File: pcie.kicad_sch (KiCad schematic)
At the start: 14 parts, among them J9 PCB-Edge_M.2_Key-M

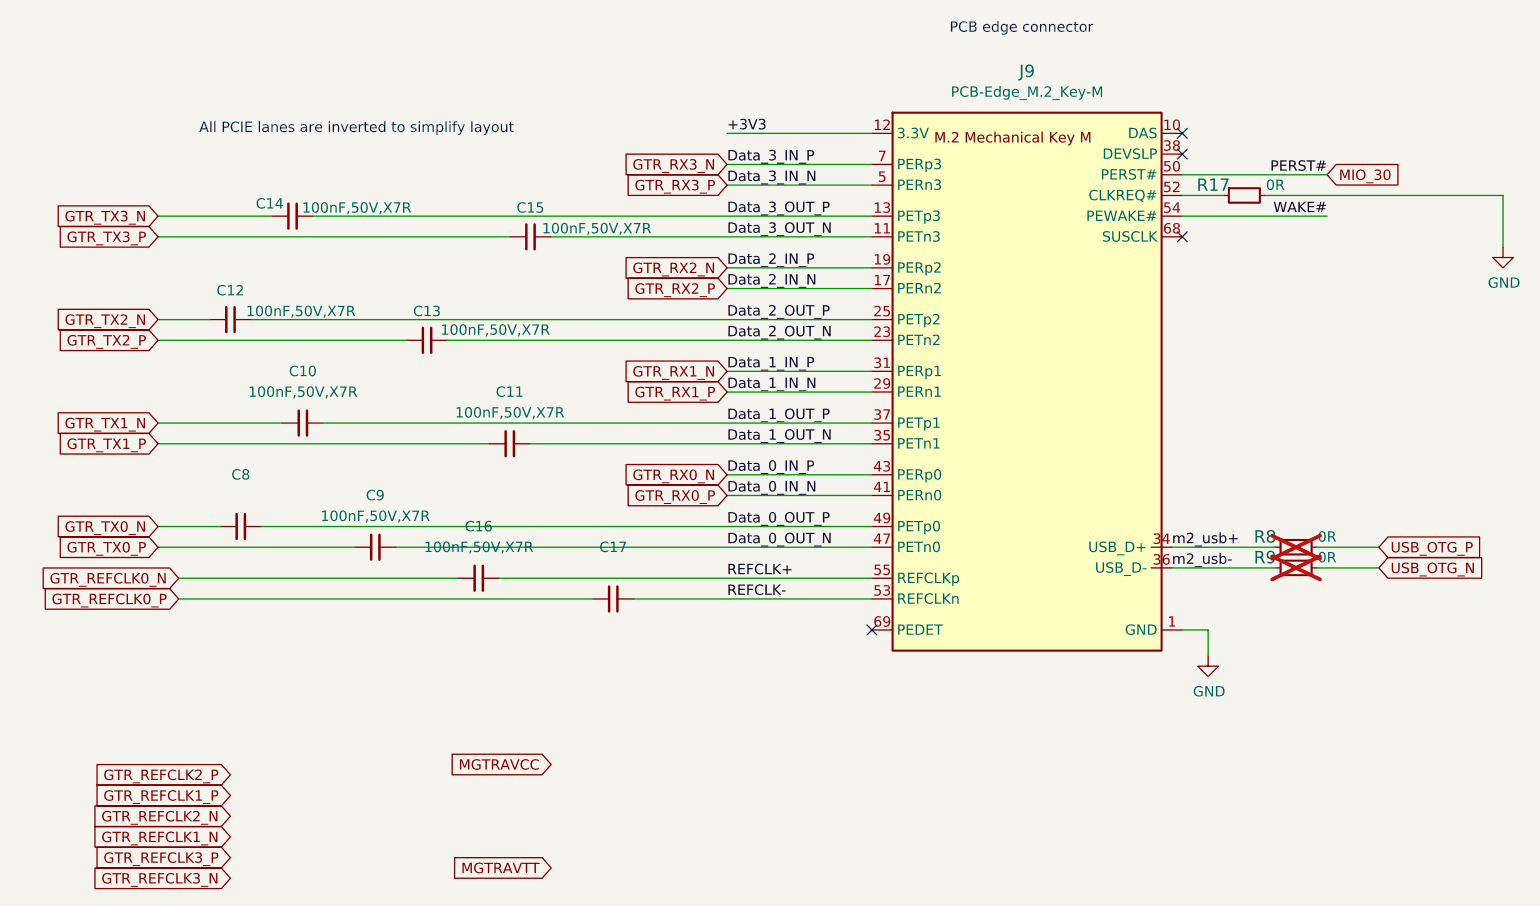
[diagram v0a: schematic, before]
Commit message: moved jtag connector, added holes for all power supplies, fixed most of DRC
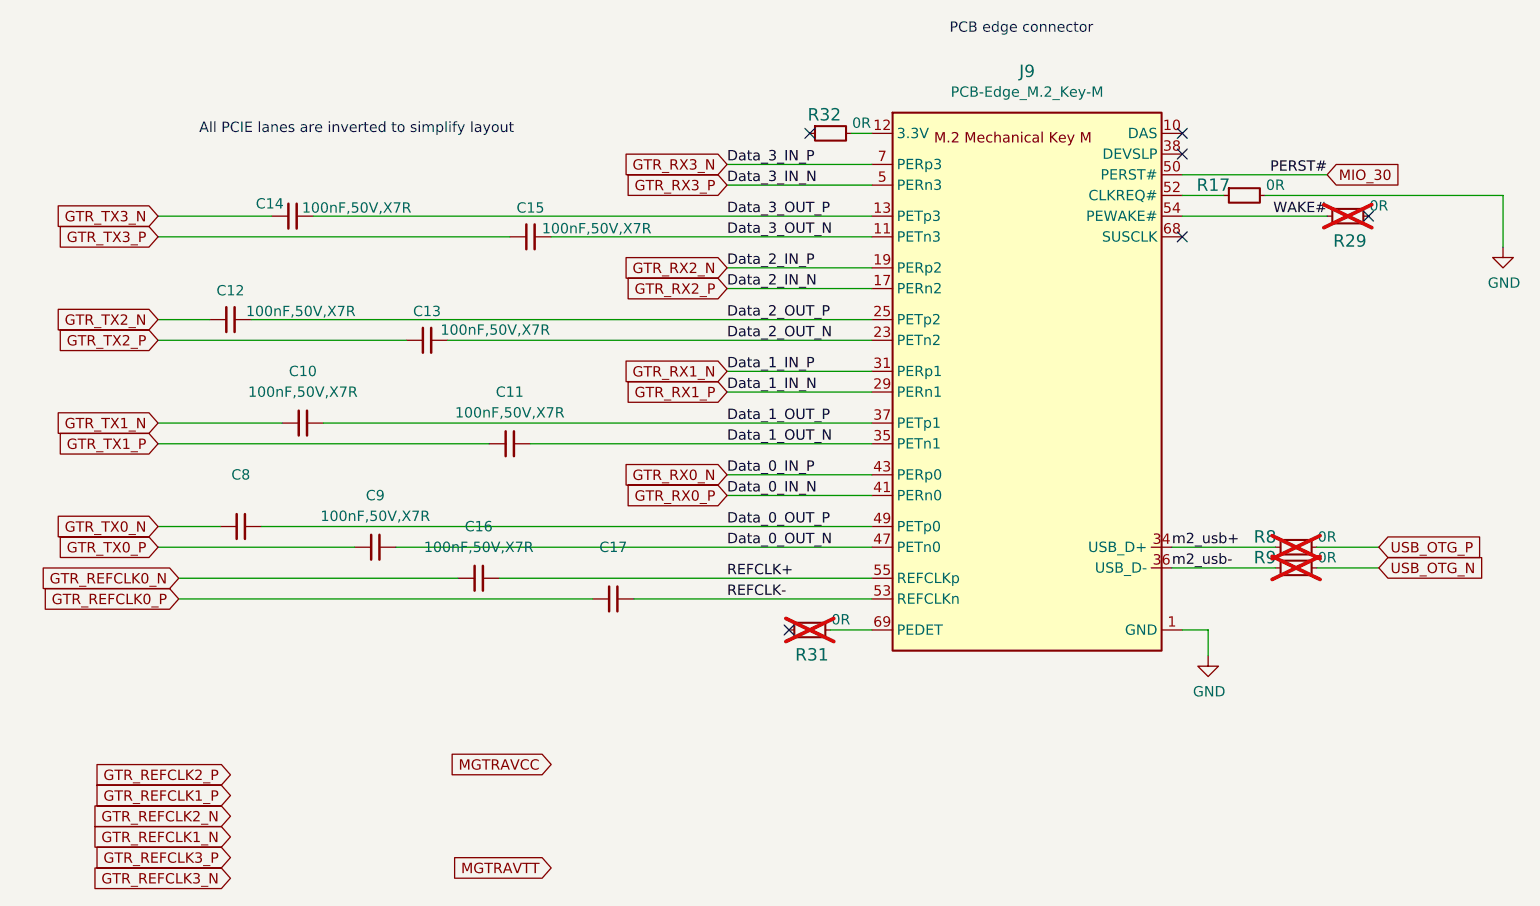
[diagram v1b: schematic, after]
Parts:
- added R29, R31, R32: R_0R_0402, Resistor_SMD:R_0402_1005Metric_Pad0.72x0.64mm_HandSolder, symbol antmicroResistors0402:R_0R_0402
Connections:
- net WAKE#: now also R29.1
- net at J9.69 (PEDET): now also R31.2
- net +3V3: no longer names the net of J9.12 (3.3V), J9.14 (3.3V), J9.16 (3.3V), J9.18 (3.3V), J9.2 (3.3V), J9.4 (3.3V), J9.70 (3.3V), J9.72 (3.3V), J9.74 (3.3V)
- net +3V3: now also R32.2
- no-connect marks 4 -> 6
